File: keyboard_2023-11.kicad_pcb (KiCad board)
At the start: 2 copper layers, 253.3 x 100.4 mm, 72 parts, among them J1 Conn_01x04, J11 Conn_01x07_Socket, J2 Conn_01x04_Socket, J3 Conn_01x07_Socket, J4 Conn_01x07_Pin, SW1 SW_Push, SW10 SW_Push, SW11 SW_Push, SW12 SW_Push, SW13 SW_Push, SW14 SW_Push, SW15 SW_Push, SW16 SW_Push, SW17 SW_Push, SW18 SW_Push, SW19 SW_Push, SW2 SW_Push, SW20 SW_Push, SW21 SW_Push, SW22 SW_Push, SW23 SW_Push, SW24 SW_Push, SW3 SW_Push, SW4 SW_Push, SW5 SW_Push, SW6 SW_Push, SW7 SW_Push, SW8 SW_Push, SW9 SW_Push, U1 MCP23017_SO, U2 MCP23017_SO

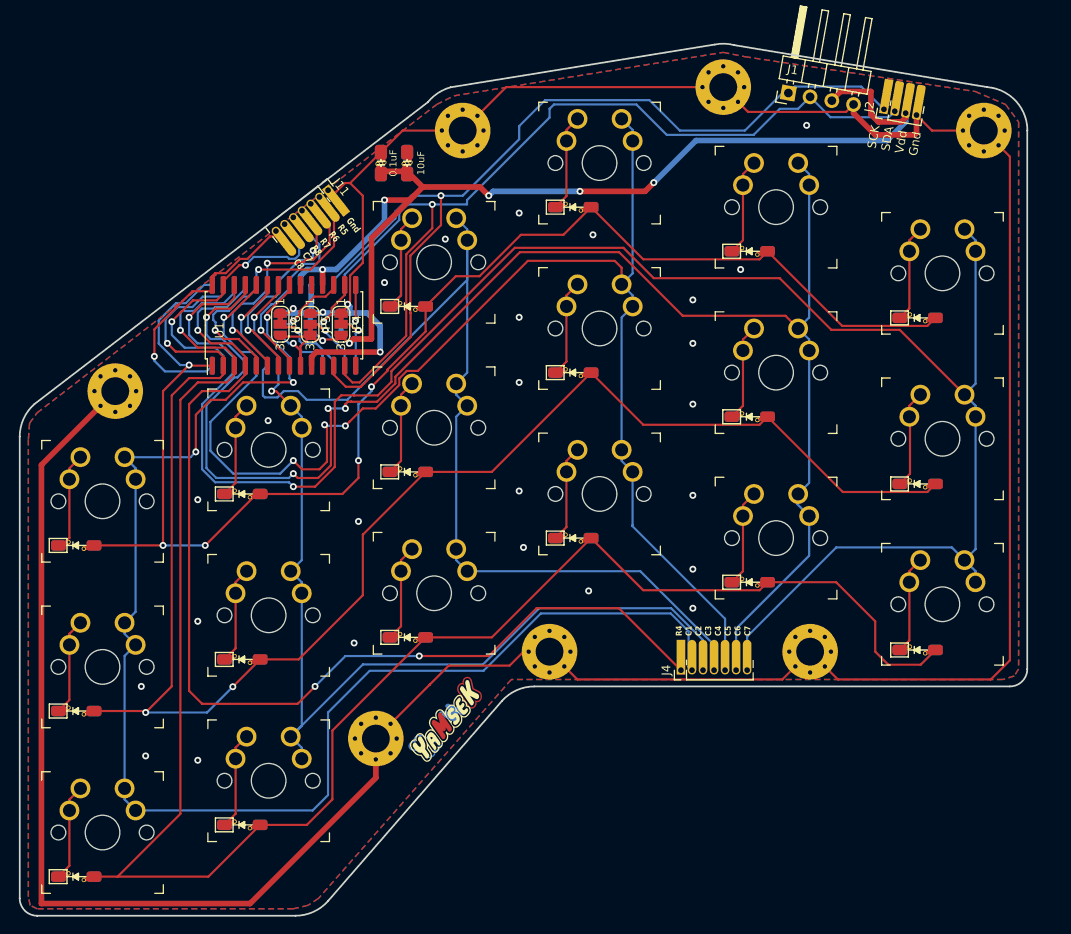
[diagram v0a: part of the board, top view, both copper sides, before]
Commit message: closing gapts:
noticed a gap on the manufactured pcb between index and middlefinger columns

=> shifted evertything a milimeter closer together
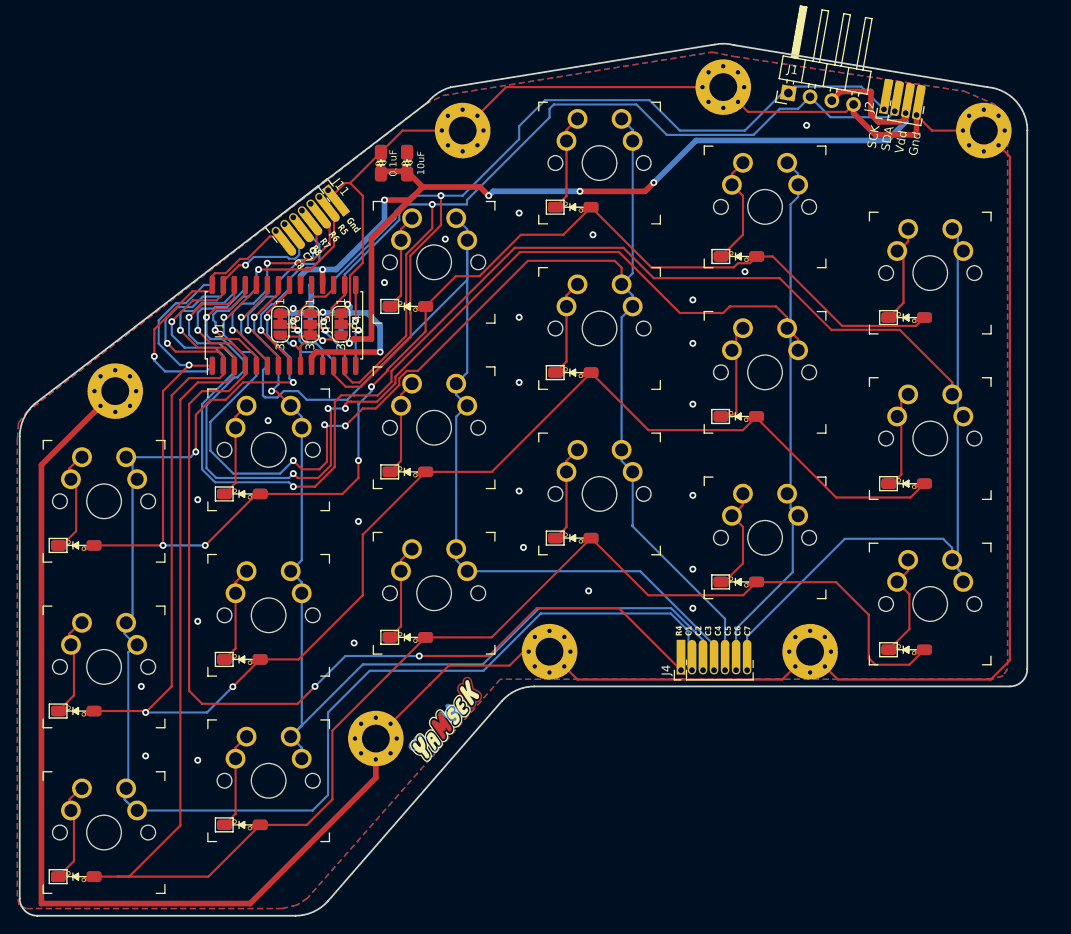
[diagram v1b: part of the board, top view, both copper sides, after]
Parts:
- moved SW12 1.41 mm to (133.8, 65.5)
- moved SW18 1.41 mm to (133.8, 84.5)
- moved SW6 1.41 mm to (133.8, 46.4)
- moved D5 1.39 mm to (111.8, 44.5)
- moved D12 1.27 mm to (131.1, 70.7)
- moved D18 1.27 mm to (131.1, 89.8)
- moved D6 1.27 mm to (131.1, 51.5)
- moved D11 1.27 mm to (111.8, 62.9)
- moved D17 1.27 mm to (111.8, 82.0)
- moved SW17 1.27 mm to (114.8, 76.9)
- moved SW5 1.27 mm to (114.8, 38.8)
- moved SW11 1.27 mm to (114.8, 57.8)
- moved SW1 0.18 mm to (38.7, 72.7)
- moved SW13 0.18 mm to (38.7, 110.8)
- moved SW7 0.18 mm to (38.7, 91.8)
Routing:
- net COL6: track 219.5 -> 217.0 mm
- net Net-(D5-K): track 11.2 -> 12.8 mm
- net COL5: track 182.8 -> 183.9 mm
- net Net-(D18-K): track 11.3 -> 12.4 mm
- net ROW1: track 166.2 -> 165.2 mm
- net Net-(D17-K): track 11.2 -> 12.1 mm
- net ROW3: track 212.1 -> 213.0 mm
- net Net-(D6-K): track 11.2 -> 11.8 mm
- net Net-(D1-K): track 11.0 -> 11.7 mm
- net Net-(D11-K): track 11.2 -> 10.7 mm

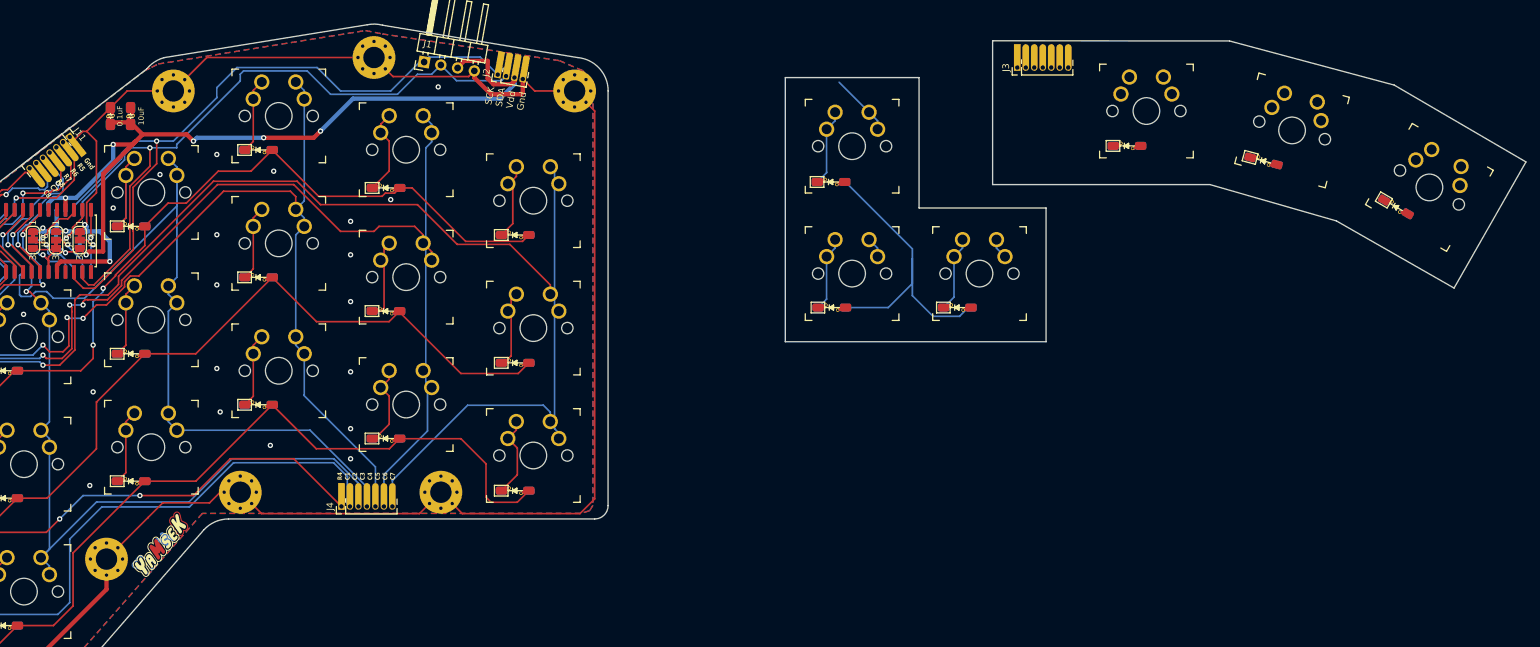
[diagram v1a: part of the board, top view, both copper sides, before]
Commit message: moved column 3 1mm down
added thumbcluster "port" (draft)
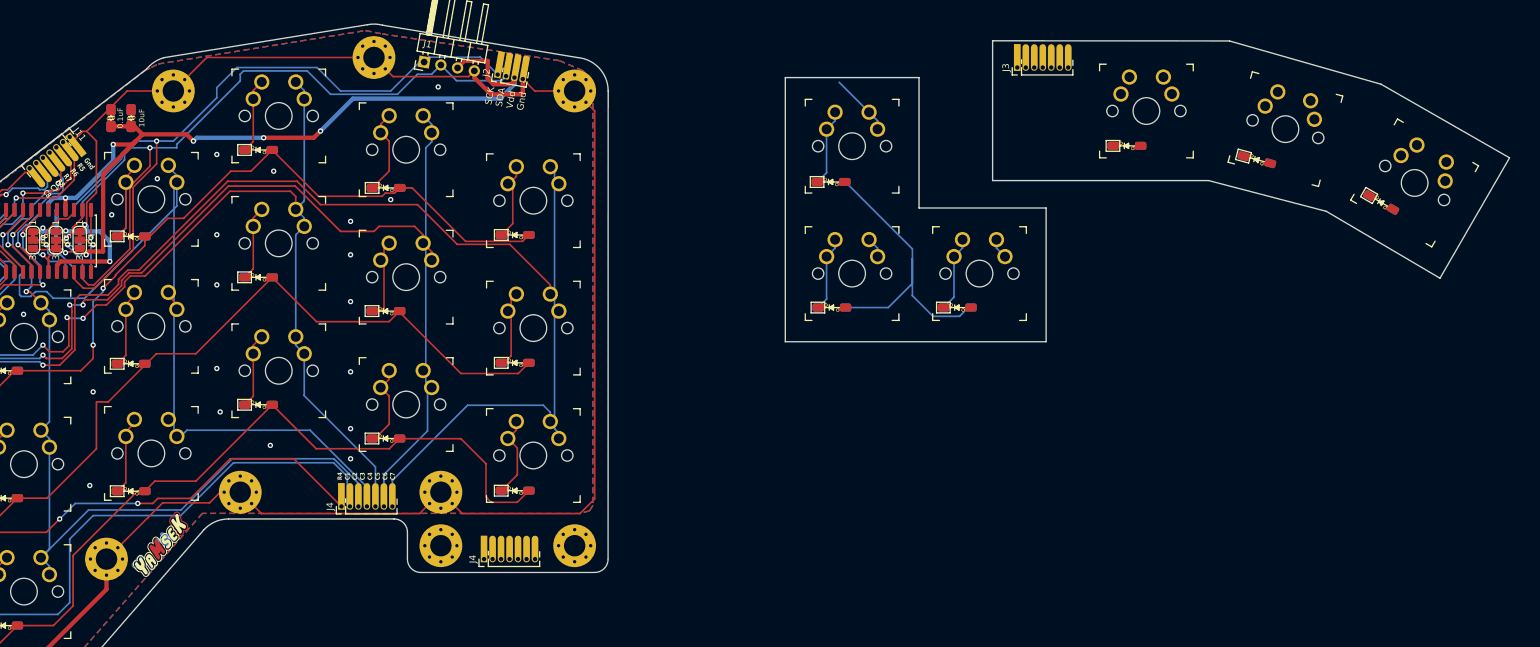
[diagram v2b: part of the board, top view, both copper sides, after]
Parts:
- added H6: MountingHole_Pad, project-local:MountingHole_3.2mm_M3_Pad_Via, F.Cu at (140.0, 98.0)
- added H6: MountingHole_Pad, project-local:MountingHole_3.2mm_M3_Pad_Via, F.Cu at (120.0, 98.0)
- added J4: Conn_01x07_Pin, project-local:PinHeader_1x07_P1.27mm_Vertical, F.Cu at (126.5, 100.0)
- moved SW24 2.31 mm to (265.6, 43.8)
- moved D24 2.31 mm to (260.6, 46.7)
- moved D15 1.50 mm to (73.7, 89.8)
- moved D3 1.50 mm to (73.7, 51.8)
- moved D9 1.50 mm to (73.7, 70.8)
- moved SW3 1.03 mm to (76.7, 46.2)
- moved D23 1.01 mm to (242.0, 40.3)
- moved SW23 1.01 mm to (246.3, 35.7)
- moved SW9 0.98 mm to (76.7, 65.2)
- moved SW15 0.93 mm to (76.7, 84.2)
- moved C2 0.31 mm to (73.7, 34.1)
- moved C1 0.31 mm to (70.7, 34.1)
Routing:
- net COL3: track 129.1 -> 130.4 mm
- net ROW1: track 165.2 -> 163.9 mm
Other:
- board size 253.3 x 100.4 mm -> 250.8 x 100.4 mm

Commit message: V2: gerber 2 JLCPCB
additional i2c ports
mounting "tab" for thumb cluster
nudged rows 3 (ringfinter) and 4 (middlefinger) a bit down
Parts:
- removed the H1 at (110.0, 25.0)
- removed the H6 at (120.0, 90.0)
- removed J1: Conn_01x04, Connector_PinHeader_2.54mm:PinHeader_1x04_P2.54mm_Horizontal
- removed the J4 at (126.5, 100.0)
- added H10: MountingHole_Pad, project-local:MountingHole_3.2mm_M3_Pad_Via, F.Cu at (189.7, 93.1)
- added H8: MountingHole_Pad, project-local:MountingHole_3.2mm_M3_Pad_Via, F.Cu at (110.0, 90.0)
- added H9: MountingHole_Pad, project-local:MountingHole_3.2mm_M3_Pad_Via, F.Cu at (189.7, 85.2)
- added J5: Conn_01x04_Socket, project-local:PinHeader_1x04_P1.27mm_Vertical, F.Cu at (140.0, 53.1)
- added J6: Conn_01x07_Pin, project-local:PinHeader_1x07_P1.27mm_Vertical, F.Cu at (169.2, 83.1)
- added J7: Conn_01x04_Socket, project-local:PinHeader_1x04_P1.27mm_Vertical, F.Cu at (98.1, 91.0)
- moved J4 22.2 mm to (126.2, 99.0)
- moved J2 3.49 mm to (126.0, 30.0), turned to 90 degrees
- moved D10 0.50 mm to (92.7, 58.4)
- moved D16 0.50 mm to (92.7, 77.4)
- moved D4 0.50 mm to (92.7, 39.3)
- moved SW10 0.50 mm to (95.8, 53.3)
- moved SW16 0.50 mm to (95.8, 72.3)
- moved SW4 0.50 mm to (95.8, 34.2)
- renumbered H5 to H1, H9 to H11, H8 to H12, H7 to H5, H6 to H7
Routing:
- net SCK: track 109.1 -> 228.1 mm, vias 1 -> 3
- net SDA: track 105.6 -> 223.4 mm, vias 1 -> 3
- net VDD: track 148.2 -> 233.4 mm, vias 8 -> 7
- net GND: track 390.8 -> 443.5 mm, vias 29 -> 54
- net ROW4: track 123.5 -> 155.7 mm
- net COL2: track 119.6 -> 145.1 mm
- net COL1: track 166.2 -> 191.0 mm
- net COL3: track 130.4 -> 153.6 mm
- net COL4: track 161.2 -> 184.1 mm
- net COL6: track 216.7 -> 201.9 mm
- net COL5: track 183.8 -> 194.6 mm
- net Net-(J3-Pin_4): track 9.40 -> 3.07 mm
- net ROW3: track 213.0 -> 211.3 mm
- net Net-(D4-K): track 11.2 -> 11.8 mm
- net Net-(D16-K): track 11.2 -> 11.7 mm
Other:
- board size 250.8 x 100.4 mm -> 250.8 x 97.9 mm

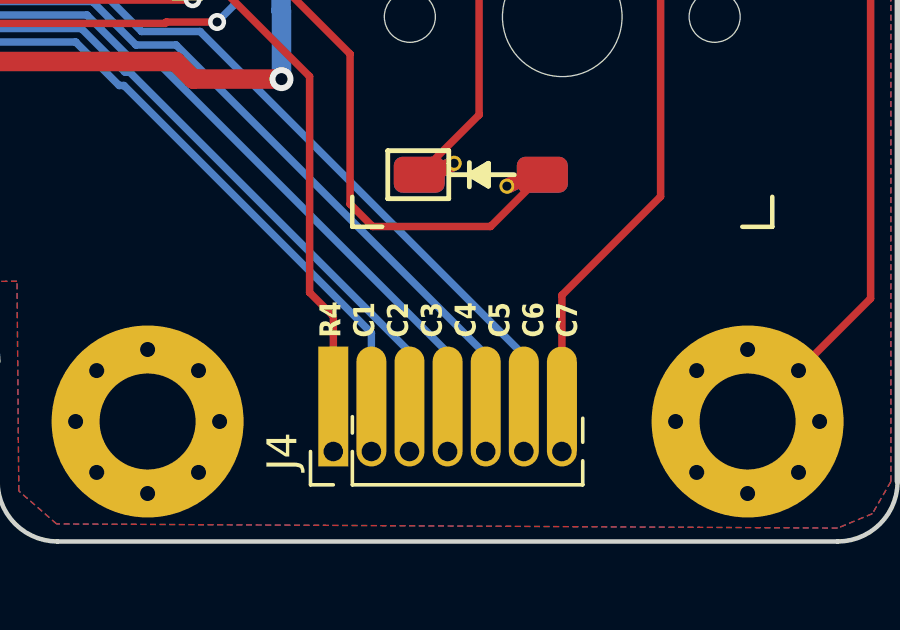
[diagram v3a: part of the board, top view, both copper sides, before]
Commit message: remove wrong 'C7' from silkscreen labels
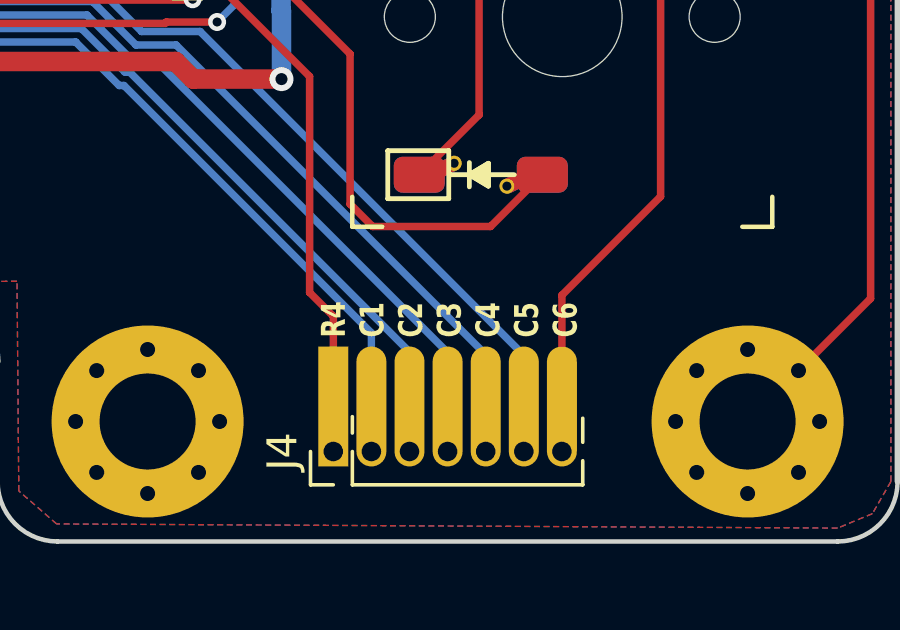
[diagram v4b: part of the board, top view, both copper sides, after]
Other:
- board text added: "R4 C1 C2 C3 C4 C5 C6"
- board text removed: "R4 C1 C2 C3 C4 C5 C6 C7"
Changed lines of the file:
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@@
     (effects (font (size 0.8 0.6) (thickness 0.1) bold) (justify left bottom mirror))
   )
-  (gr_text "R4\nC1\nC2\nC3\nC4\nC5\nC6\nC7" (at 134.4 93.9 90) (layer "B.SilkS")
-    (effects (font (size 0.7 0.6) (thickness 0.1) bold) (justify left bottom mirror))
+  (gr_text "R4\nC1\nC2\nC3\nC4\nC5\nC6" (at 134.4 93.9 90) (layer "B.SilkS")
+    (effects (font (size 0.8 0.6) (thickness 0.1) bold) (justify left bottom mirror))
   )
   (gr_text "SCK\nSDA\nVdd\nGnd" (at 103.027478 87.091571 90) (layer "F.SilkS")
@@
     (effects (font (size 0.8 0.6) (thickness 0.1) bold) (justify left bottom))
   )
-  (gr_text "R4 \nC1 \nC2 \nC3 \nC4 \nC5\nC6\nC7" (at 134.4 95.2 90) (layer "F.SilkS")
-    (effects (font (size 0.7 0.6) (thickness 0.1) bold) (justify left bottom))
+  (gr_text "R4 \nC1 \nC2 \nC3 \nC4 \nC5\nC6" (at 134.4 95.2 90) (layer "F.SilkS")
+    (effects (font (size 0.8 0.6) (thickness 0.1) bold) (justify left bottom))
   )
   (gr_text "SCK\nSDA\nVdd\nGnd" (at 130.977465 34.17688 90) (layer "F.SilkS")
